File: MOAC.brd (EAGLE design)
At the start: 113 x 40 mm, 57 parts, among them IC1 ATMEGA32U4-QFN

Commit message: Improved designators
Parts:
- C4: value 1uF 0603 -> 1uF

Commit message: Replaced parts using SuperHouse libraries to add 3D models
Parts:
- removed JP2: OLED, freetronics-jon:1X04
- removed S1, S2, S3, S4, S5, S6, S7, S8: 3.5mm, freetronics-jon:AUDIO-JACK-PJ321
- removed S21: RESET, freetronics-jon:TACTILE_SWITCH_SMD_2PIN_TINY
- removed S22: HWB, freetronics-jon:TACTILE_SWITCH_SMD_2PIN_TINY
- removed U$15: USB-C, freetronics-jon:USB-C-U52A
- added J1, J2, J3, J4, J5, J6, J7, J8: 3.5mm, SuperHouse-Connectors:AUDIO-JACK-PJ321
- added J9: USB-C, SuperHouse-Connectors:USB-C-U52A
- added MOD1: OLED-I2C128X32-0.91, SuperHouse-Displays:OLED-128X32-0.91
- added S10: HWB, SuperHouse-Switches:TACTILE_SMD_3X4X2
- added S9: RESET, SuperHouse-Switches:TACTILE_SMD_3X4X2
- C1, C2, C3, C4, C5, C6: device freetronics-master-v1.1:0603 -> SuperHouse-DiscreteSemi:C0603
- F1: device rcl:L1812 -> SuperHouse-Fuses:1812
- ICSP: device pinhead:2X03 -> SuperHouse-Connectors:2X03PTH
- JP1: device freetronics-jon:1X02 -> SuperHouse-Connectors:1X02
- LED1, LED2, LED3, LED4: device freetronics-jon:LED-0603 -> SuperHouse-LEDs:LED-0603
- PIEZO: device freetronics-master-v1:BUZZER-12X12-SMT -> SuperHouse-Audio:BUZZER-12X12-SMT
- R1, R10, R11, R12, R13, R14, R15, R16, R17, R19, R20, R21, R22, R23, R24, R25, R3, R4, R5, R6, R8, R9: device freetronics-jon:0603 -> SuperHouse-DiscreteSemi:R0603
- R18, R7: device freetronics-original:0603 -> SuperHouse-DiscreteSemi:R0603
- R2: device freetronics-master-v1.1:0603 -> SuperHouse-DiscreteSemi:R0603
- XTL1: device freetronics-jon:CRYSTAL-SMD-3X2 -> SuperHouse-Oscillators:CRYSTAL-SMD-3X2
- Z1, Z2: device freetronics-master-v1.1:0603 -> SuperHouse-DiscreteSemi:TVS0603
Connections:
- net 5V: now also MOD1.VCC; no longer JP2.3
- net D+: now also J9.A6, J9.B6; no longer U$15.A6, U$15.B6
- net D-: now also J9.A7, J9.B7; no longer U$15.A7, U$15.B7
- net D2_SDA: now also MOD1.SDA; no longer JP2.1
- net D3_SCL: now also MOD1.SCL; no longer JP2.2
- net GND: now also J1.3, J2.3, J3.3, J4.3, J5.3, J6.3, J7.3, J8.3, J9.A1, J9.A12, J9.B1, J9.B12, J9.CASE1, J9.CASE2, J9.CASE3, J9.CASE4, J9.FIX1, J9.FIX2, J9.FIX3, J9.FIX4, MOD1.GND, S10.2, S9.1; no longer JP2.4, S1.3, S2.3, S21.1, S22.2, S3.3, S4.3, S5.3, S6.3, S7.3, S8.3, U$15.A1, U$15.A12, U$15.B1, U$15.B12, U$15.CASE1, U$15.CASE2, U$15.CASE3, U$15.CASE4, U$15.FIX1, U$15.FIX2, U$15.FIX3, U$15.FIX4
- net HWB: now also S10.1; no longer S22.1
- net N$1: now also J9.B5; no longer U$15.B5
- net N$10: now also J5.4A, J5.4B; no longer S5.4A, S5.4B
- net N$13: now also J6.4A, J6.4B; no longer S6.4A, S6.4B
- net N$14: now also J7.4A, J7.4B; no longer S7.4A, S7.4B
- net N$15: now also J8.4A, J8.4B; no longer S8.4A, S8.4B
- net N$3: now also J1.4A, J1.4B; no longer S1.4A, S1.4B
- net N$4: now also J2.4A, J2.4B; no longer S2.4A, S2.4B
- net N$5: now also J3.4A, J3.4B; no longer S3.4A, S3.4B
- net N$67: now also J9.A5; no longer U$15.A5
- net N$9: now also J4.4A, J4.4B; no longer S4.4A, S4.4B
- net RESET: now also S9.2; no longer S21.2
- net USB+: now also J9.A4, J9.A9, J9.B4, J9.B9; no longer U$15.A4, U$15.A9, U$15.B4, U$15.B9
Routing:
- net 5V: track 362.3 -> 356.3 mm
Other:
- board text added: "v1.1"
- board text removed: "v1.0"

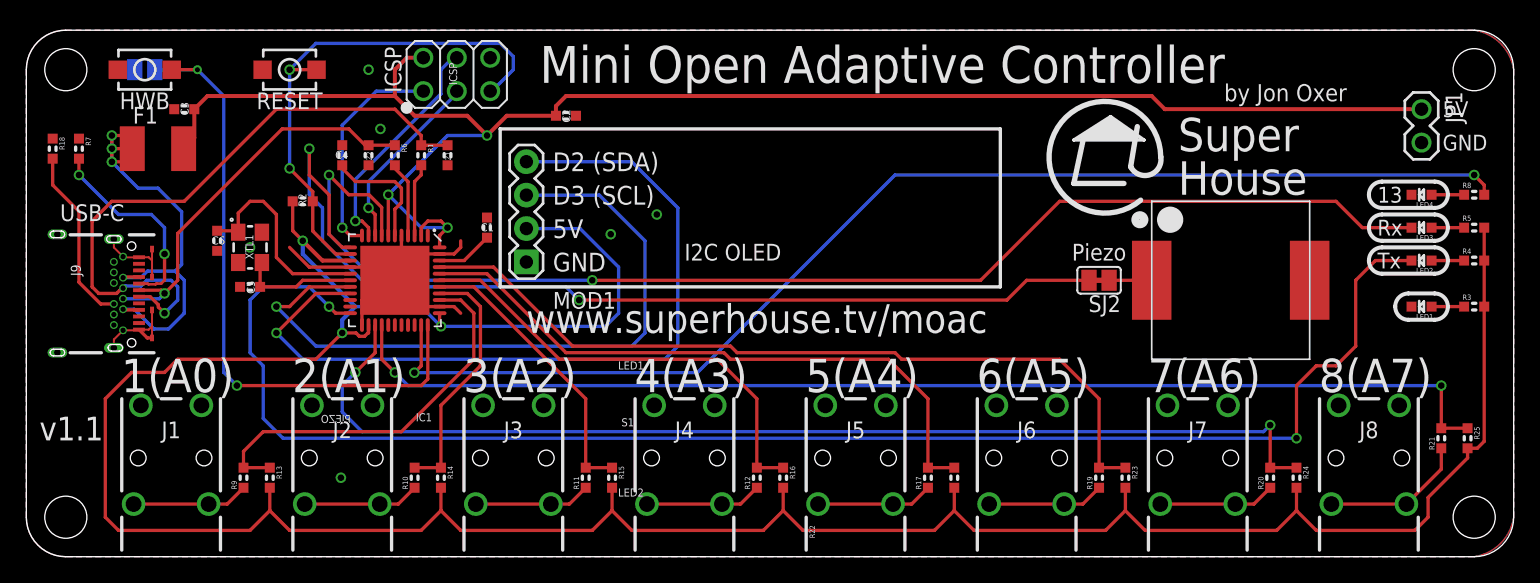
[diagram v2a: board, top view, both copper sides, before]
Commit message: Replaced 128x32 OLED with 128x64, 1.3in for v2.0 release
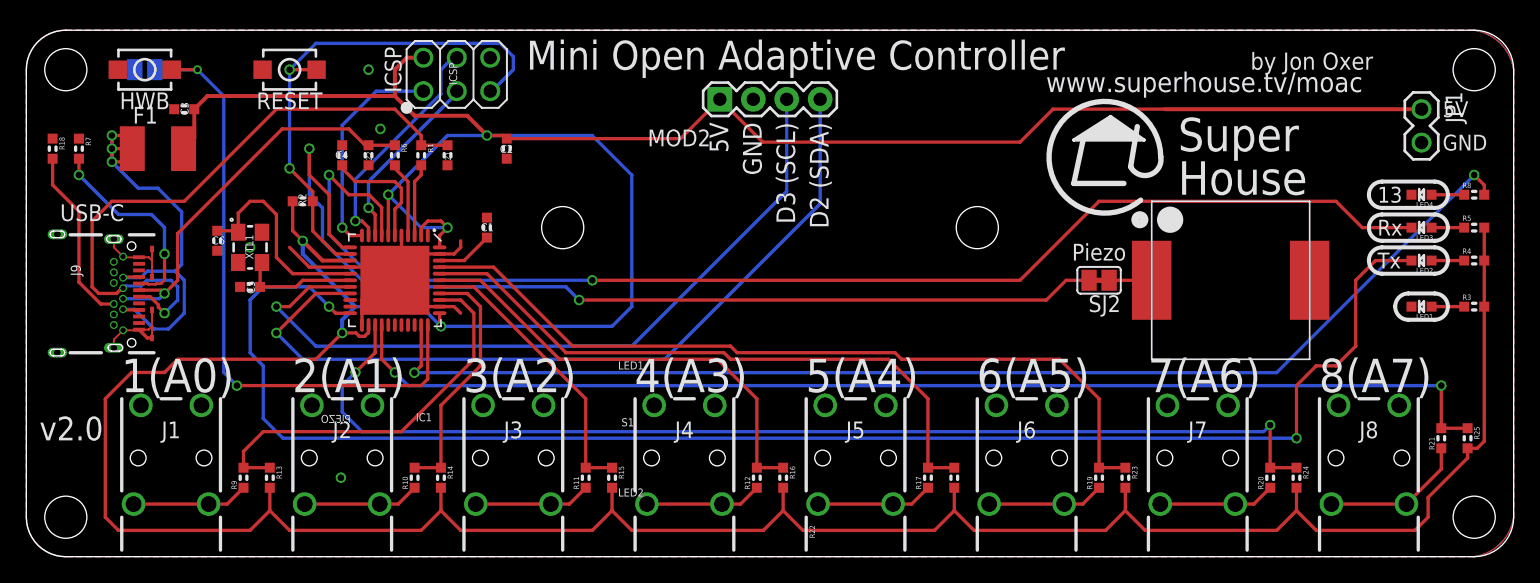
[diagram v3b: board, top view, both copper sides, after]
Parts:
- removed MOD1: OLED-I2C128X32-0.91, SuperHouse-Displays:OLED-128X32-0.91
- added MOD2: OLED-I2C128X64-1.3-HO, SuperHouse-Displays:OLED-128X64-1.3-HO
- moved C2 5.15 mm to (36.5, 31.0), turned to 270 degrees
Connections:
- net 5V: now also MOD2.VCC; no longer MOD1.VCC
- net D2_SDA: now also MOD2.SDA; no longer MOD1.SDA
- net D3_SCL: now also MOD2.SCL; no longer MOD1.SCL
- net GND: now also MOD2.GND; no longer MOD1.GND
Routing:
- net 5V: track 356.3 -> 369.7 mm
- net D3_SCL: track 53.3 -> 58.1 mm
- net GND: vias 6 -> 4
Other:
- board text added: "v2.0"
- board text removed: "I2C OLED"
- board text removed: "v1.1"

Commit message: Changed ATmega32U4 from QFN to TQFP to save Jon's sanity for v2.0 release
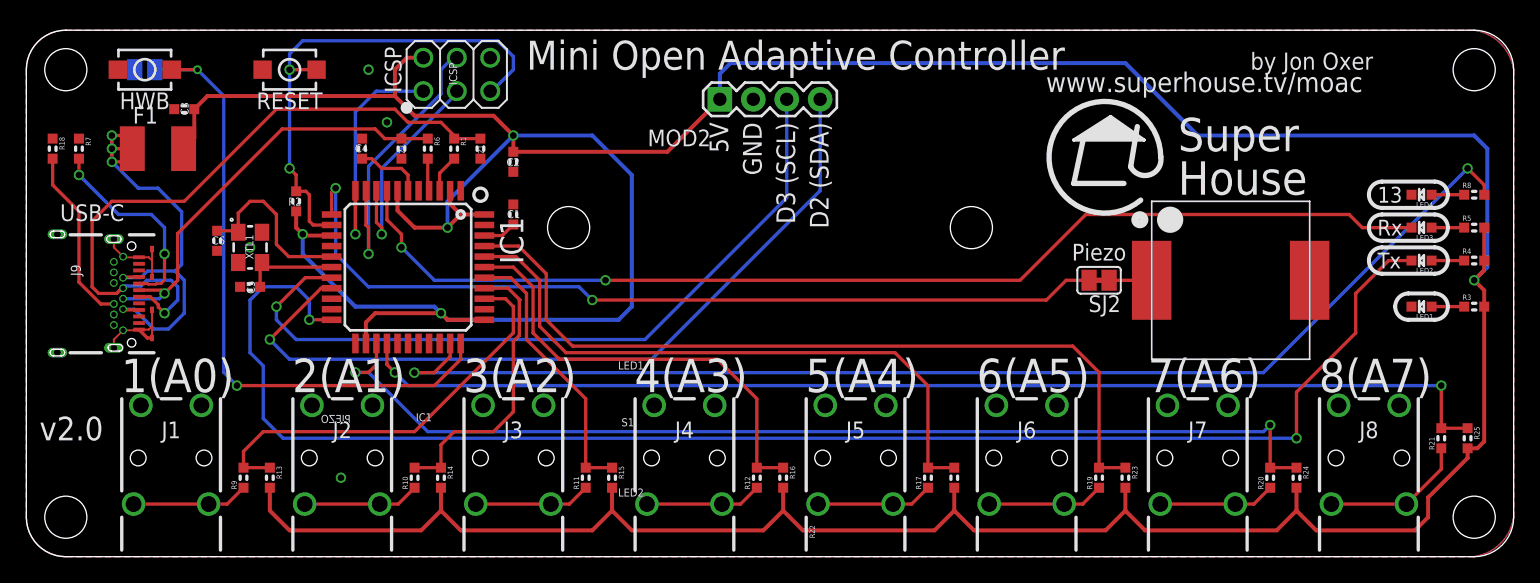
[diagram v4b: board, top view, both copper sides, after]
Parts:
- removed JP1: 5V, SuperHouse-Connectors:1X02
- IC1: value ATMEGA32U4-QFN -> ATMEGA32U4NT-TQFP; device freetronics-jon:QFN-44N -> SuperHouse-MCUs:TQFP44
- SJ1: device freetronics-jon:SJ -> SuperHouse-Jumpers:SJ
- SJ2: device freetronics-jon:SJC -> SuperHouse-Jumpers:SJC
- moved R1 2.55 mm to (32.5, 31.0)
- moved R6 2.55 mm to (30.5, 31.0)
- moved Z1 2.55 mm to (34.5, 31.0)
- moved Z2 2.55 mm to (28.5, 31.0)
- moved C1 2.24 mm to (37.0, 26.0)
- moved C4 1.58 mm to (25.5, 31.0)
- moved IC1 1.41 mm to (29.0, 22.0), turned to 270 degrees
- moved C2 1.12 mm to (37.0, 30.0)
- moved R2 0.50 mm to (20.5, 27.0), turned to 270 degrees
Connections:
- net 5V: no longer JP1.1
- net GND: no longer IC1.TGND, JP1.2
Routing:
- net GND: track 42.2 -> 13.3 mm
- net 5V: track 369.7 -> 344.3 mm, vias 6 -> 5
- net RXLED_SS: track 98.7 -> 85.0 mm
- net D11: track 77.3 -> 66.4 mm
- net MOSI: track 17.6 -> 22.7 mm
- net 3V3: track 9.17 -> 5.21 mm
- net D4_A6: track 84.2 -> 80.3 mm
- net RD+: track 5.75 -> 2.48 mm
- net A1: track 19.0 -> 22.1 mm
- net SCK: track 14.0 -> 16.7 mm
- net RD-: track 5.55 -> 2.89 mm
- net N$12: track 16.5 -> 14.0 mm
- net D+: track 30.6 -> 32.9 mm
- net D-: track 49.4 -> 51.4 mm
- net TX_LED: track 117.0 -> 115.2 mm
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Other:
- board text added: "Arduino "Leonardo" Compatible"
- board text added: "Copyright 2018-2019 SuperHouse Automation Pty Ltd Released under the TAPR Open Hardware License www.tapr.org/OHL"
- board text added: "Display: 128x64 OLED I2C SH1106 controller"
- board text removed: "Arduino Leonardo Compatible"
- board text removed: "Copyright 2018 SuperHouse Automation Pty Ltd Released under the TAPR Open Hardware License www.tapr.org/OHL"
